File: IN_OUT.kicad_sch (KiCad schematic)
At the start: 37 parts, among them J3 Conn_DEGSON_01x02_Pin, J4 Conn_DEGSON_01x02_Pin, J5 Conn_DEGSON_01x02_Pin, J6 Conn_DEGSON_01x02_Pin, J7 Conn_DEGSON_01x02_Pin, U2 PRAG71S, U3 PRAG71S, U4 PRAG71S, U5 PRAG71S

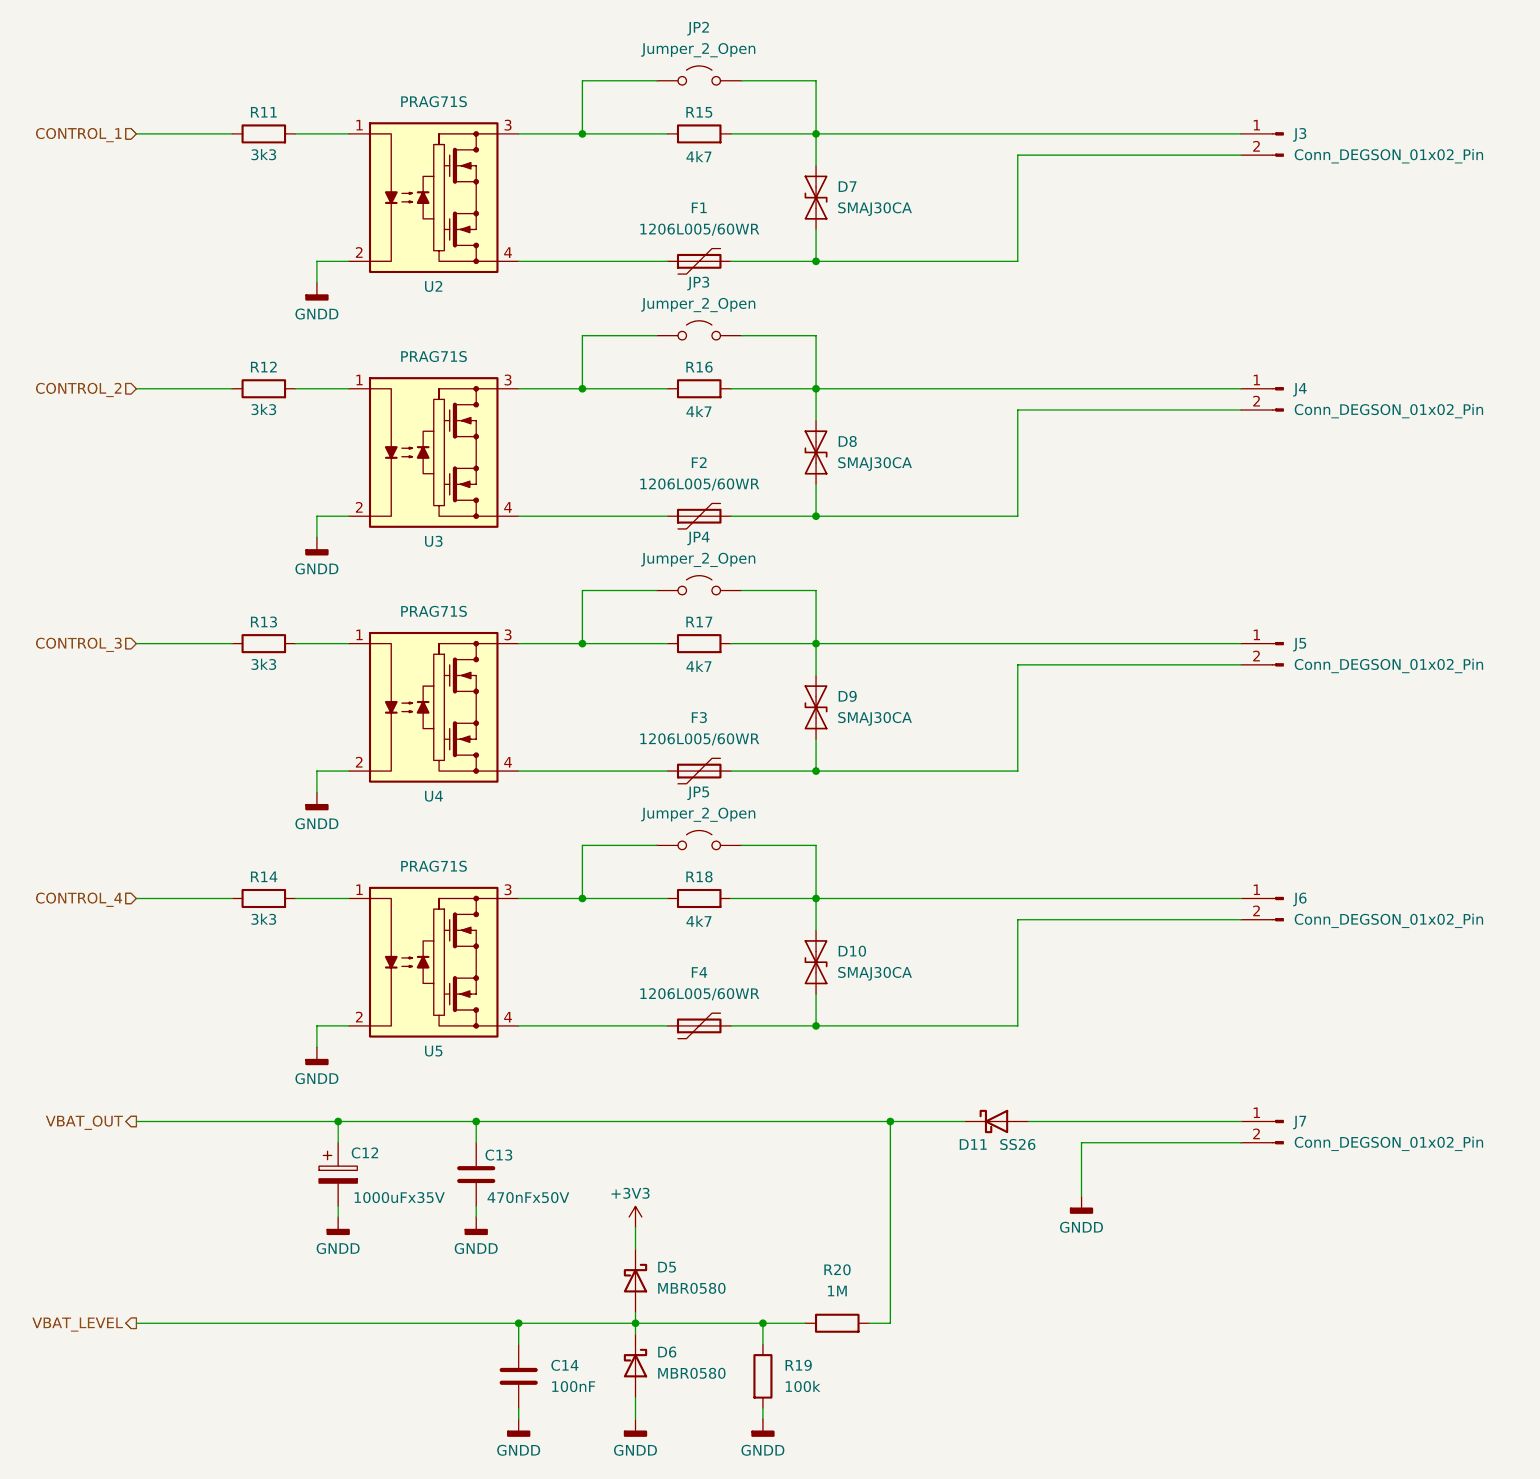
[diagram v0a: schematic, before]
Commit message: Move to SIM800C-DS and two SIM
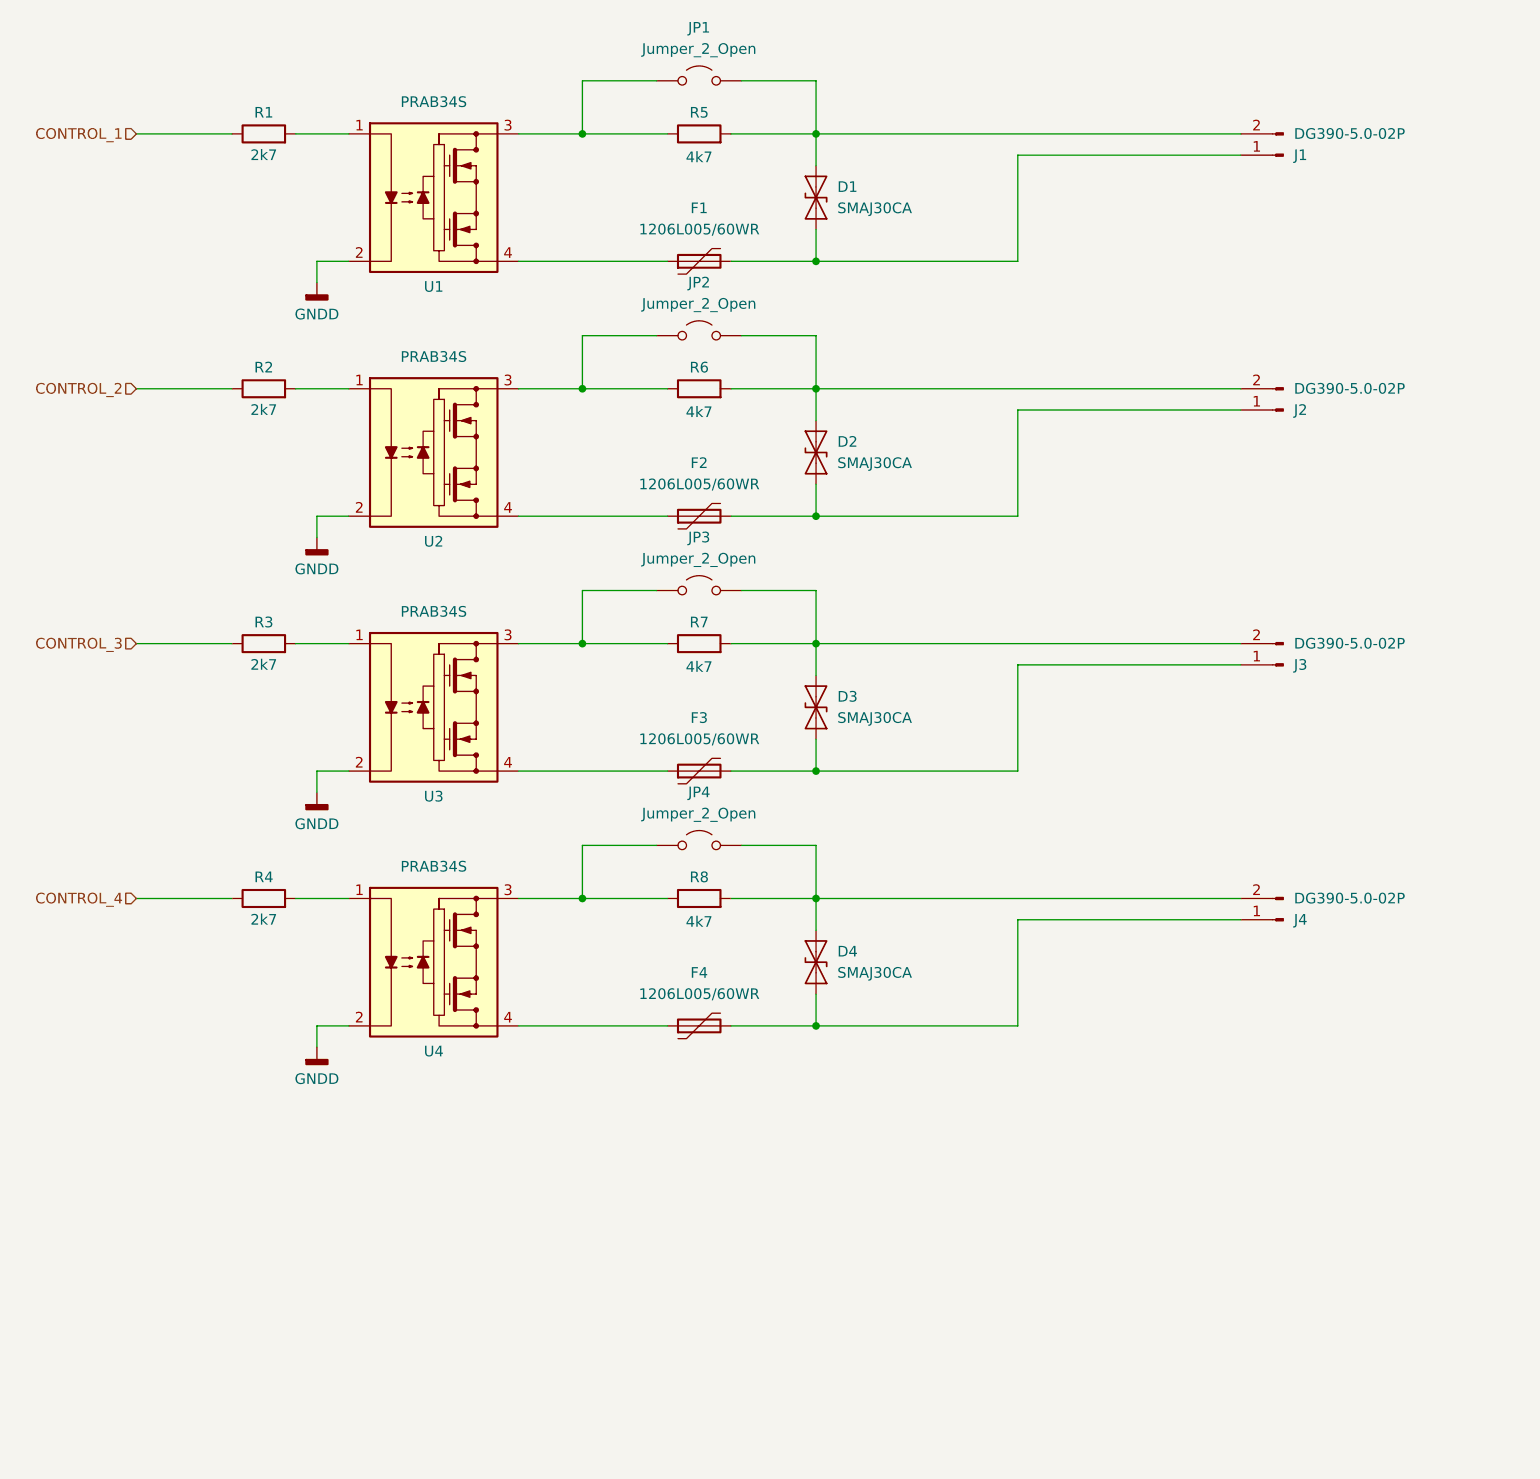
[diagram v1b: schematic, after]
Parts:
- removed C12: 1000uFx35V, Capacitor_THT:CP_Radial_D12.5mm_P5.00mm, symbol Device:C_Polarized
- removed C13: 470nFx50V, Capacitor_SMD:C_0805_2012Metric_Pad1.18x1.45mm_HandSolder, symbol Device:C
- removed C14: 100nF, Capacitor_SMD:C_0805_2012Metric_Pad1.18x1.45mm_HandSolder, symbol Device:C
- removed D11: SS26, Diode_SMD:D_SMA, symbol Diode:SS26
- removed D5, D6: MBR0580, Diode_SMD:D_SOD-123, symbol Diode:MBR0580
- removed J7: Conn_DEGSON_01x02_Pin, footprints:DEGSON_DG390-5.0-02P_1x02_P5.0mm_Vertical, symbol symbols:Conn_DEGSON_01x02_Pin
- removed R19: 100k, Resistor_SMD:R_0805_2012Metric_Pad1.20x1.40mm_HandSolder, symbol Device:R
- removed R20: 1M, Resistor_SMD:R_0805_2012Metric_Pad1.20x1.40mm_HandSolder, symbol Device:R
- D1: renamed from D7; MPN (none) -> SMAJ30CA; Manufacturer (none) -> Littelfuse
- D2: renamed from D8; MPN (none) -> SMAJ30CA; Manufacturer (none) -> Littelfuse
- D3: renamed from D9; MPN (none) -> SMAJ30CA; Manufacturer (none) -> Littelfuse
- D4: renamed from D10; MPN (none) -> SMAJ30CA; Manufacturer (none) -> Littelfuse
- F1, F2, F3, F4: MPN (none) -> 1206L005/60WR; Manufacturer (none) -> Littelfuse
- J1: renamed from J3; value Conn_DEGSON_01x02_Pin -> DG390-5.0-02P; MPN (none) -> DG390-5.0-02P; Manufacturer (none) -> NINGBO DEGSON ELECTRICAL CO.,LTD.
- J2: renamed from J4; value Conn_DEGSON_01x02_Pin -> DG390-5.0-02P; MPN (none) -> DG390-5.0-02P; Manufacturer (none) -> NINGBO DEGSON ELECTRICAL CO.,LTD.
- J3: renamed from J5; value Conn_DEGSON_01x02_Pin -> DG390-5.0-02P; MPN (none) -> DG390-5.0-02P; Manufacturer (none) -> NINGBO DEGSON ELECTRICAL CO.,LTD.
- J4: renamed from J6; value Conn_DEGSON_01x02_Pin -> DG390-5.0-02P; MPN (none) -> DG390-5.0-02P; Manufacturer (none) -> NINGBO DEGSON ELECTRICAL CO.,LTD.
- JP1: renamed from JP2; MPN (none) -> DS1021-1x2SF11-B; Manufacturer (none) -> CONNFLY ELECTRONIC CO. LTD
- JP2: renamed from JP3; MPN (none) -> DS1021-1x2SF11-B; Manufacturer (none) -> CONNFLY ELECTRONIC CO. LTD
- JP3: renamed from JP4; MPN (none) -> DS1021-1x2SF11-B; Manufacturer (none) -> CONNFLY ELECTRONIC CO. LTD
- JP4: renamed from JP5; MPN (none) -> DS1021-1x2SF11-B; Manufacturer (none) -> CONNFLY ELECTRONIC CO. LTD
- R1: renamed from R11; value 3k3 -> 2k7; MPN (none) -> RC0805JR-072K7L; Manufacturer (none) -> YAGEO
- R2: renamed from R12; value 3k3 -> 2k7; MPN (none) -> RC0805JR-072K7L; Manufacturer (none) -> YAGEO
- R3: renamed from R13; value 3k3 -> 2k7; MPN (none) -> RC0805JR-072K7L; Manufacturer (none) -> YAGEO
- R4: renamed from R14; value 3k3 -> 2k7; MPN (none) -> RC0805JR-072K7L; Manufacturer (none) -> YAGEO
- R5: renamed from R15; MPN (none) -> RC0805JR-134K7L; Manufacturer (none) -> YAGEO
- R6: renamed from R16; MPN (none) -> RC0805JR-134K7L; Manufacturer (none) -> YAGEO
- R7: renamed from R17; MPN (none) -> RC0805JR-134K7L; Manufacturer (none) -> YAGEO
- R8: renamed from R18; MPN (none) -> RC0805JR-134K7L; Manufacturer (none) -> YAGEO
- U1: renamed from U2; value PRAG71S -> PRAB34S; MPN (none) -> PRAB34S; Manufacturer (none) -> АО "Протон"
- U2: renamed from U3; value PRAG71S -> PRAB34S; MPN (none) -> PRAB34S; Manufacturer (none) -> АО "Протон"
- U3: renamed from U4; value PRAG71S -> PRAB34S; MPN (none) -> PRAB34S; Manufacturer (none) -> АО "Протон"
- U4: renamed from U5; value PRAG71S -> PRAB34S; MPN (none) -> PRAB34S; Manufacturer (none) -> АО "Протон"
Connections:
- net at D3.1 (A1), F3.2: now also J3.1 (Pin_1); no longer J3.2 (Pin_2)
- net at D4.1 (A1), F4.2: now also J4.1 (Pin_1); no longer J4.2 (Pin_2)
- net at D4.2 (A2), JP4.2 (B), R8.2: now also J4.2 (Pin_2); no longer J4.1 (Pin_1)
- net at D3.2 (A2), JP3.2 (B), R7.2: now also J3.2 (Pin_2); no longer J3.1 (Pin_1)
- net at D2.2 (A2), JP2.2 (B), R6.2: now also J2.2 (Pin_2); no longer J2.1 (Pin_1)
- net at D1.1 (A1), F1.2: now also J1.1 (Pin_1); no longer J1.2 (Pin_2)
- net at D1.2 (A2), JP1.2 (B), R5.2: now also J1.2 (Pin_2); no longer J1.1 (Pin_1)
- net at D2.1 (A1), F2.2: now also J2.1 (Pin_1); no longer J2.2 (Pin_2)
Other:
- moved on the sheet: J1, J2, J3, J4

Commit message: Release candidate
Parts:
- JP1, JP2, JP3, JP4: footprint TestPoint:TestPoint_2Pads_Pitch2.54mm_Drill0.8mm -> Connector_PinHeader_2.54mm:PinHeader_1x02_P2.54mm_Vertical
- R5, R6, R7, R8: footprint Resistor_SMD:R_0805_2012Metric_Pad1.20x1.40mm_HandSolder -> Resistor_SMD:R_1206_3216Metric_Pad1.30x1.75mm_HandSolder; MPN RC0805JR-134K7L -> RC1206JR-074K7L
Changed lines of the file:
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@@
 (kicad_sch
-	(version 20260101)
+	(version 20260306)
 	(generator "eeschema")
 	(generator_version "10.0")
@@
 			)
 		)
-		(property "Footprint" "TestPoint:TestPoint_2Pads_Pitch2.54mm_Drill0.8mm"
+		(property "Footprint" "Connector_PinHeader_2.54mm:PinHeader_1x02_P2.54mm_Vertical"
 			(at 125.73 91.44 0)
 			(hide yes)
@@
 			)
 		)
-		(property "Footprint" "Resistor_SMD:R_0805_2012Metric_Pad1.20x1.40mm_HandSolder"
+		(property "Footprint" "Resistor_SMD:R_1206_3216Metric_Pad1.30x1.75mm_HandSolder"
 			(at 125.73 69.088 90)
 			(hide yes)
@@
 			)
 		)
-		(property "MPN" "RC0805JR-134K7L"
+		(property "MPN" "RC1206JR-074K7L"
 			(at 125.73 67.31 90)
 			(hide yes)
@@
 			)
 		)
-		(property "Footprint" "TestPoint:TestPoint_2Pads_Pitch2.54mm_Drill0.8mm"
+		(property "Footprint" "Connector_PinHeader_2.54mm:PinHeader_1x02_P2.54mm_Vertical"
 			(at 125.73 60.96 0)
 			(hide yes)
@@
 			)
 		)
-		(property "Footprint" "Resistor_SMD:R_0805_2012Metric_Pad1.20x1.40mm_HandSolder"
+		(property "Footprint" "Resistor_SMD:R_1206_3216Metric_Pad1.30x1.75mm_HandSolder"
 			(at 125.73 38.608 90)
 			(hide yes)
@@
 			)
 		)
-		(property "MPN" "RC0805JR-134K7L"
+		(property "MPN" "RC1206JR-074K7L"
 			(at 125.73 36.83 90)
 			(hide yes)
@@
 			)
 		)
-		(property "Footprint" "Resistor_SMD:R_0805_2012Metric_Pad1.20x1.40mm_HandSolder"
+		(property "Footprint" "Resistor_SMD:R_1206_3216Metric_Pad1.30x1.75mm_HandSolder"
 			(at 125.73 130.048 90)
 			(hide yes)
@@
 			)
 		)
-		(property "MPN" "RC0805JR-134K7L"
+		(property "MPN" "RC1206JR-074K7L"
 			(at 125.73 128.27 90)
 			(hide yes)
@@
 			)
 		)
-		(property "Footprint" "TestPoint:TestPoint_2Pads_Pitch2.54mm_Drill0.8mm"
+		(property "Footprint" "Connector_PinHeader_2.54mm:PinHeader_1x02_P2.54mm_Vertical"
 			(at 125.73 121.92 0)
 			(hide yes)
@@
 			)
 		)
-		(property "Footprint" "TestPoint:TestPoint_2Pads_Pitch2.54mm_Drill0.8mm"
+		(property "Footprint" "Connector_PinHeader_2.54mm:PinHeader_1x02_P2.54mm_Vertical"
 			(at 125.73 30.48 0)
 			(hide yes)
@@
 			)
 		)
-		(property "Footprint" "Resistor_SMD:R_0805_2012Metric_Pad1.20x1.40mm_HandSolder"
+		(property "Footprint" "Resistor_SMD:R_1206_3216Metric_Pad1.30x1.75mm_HandSolder"
 			(at 125.73 99.568 90)
 			(hide yes)
@@
 			)
 		)
-		(property "MPN" "RC0805JR-134K7L"
+		(property "MPN" "RC1206JR-074K7L"
 			(at 125.73 97.79 90)
 			(hide yes)

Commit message: Proproduction version
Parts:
- J1: value DG390-5.0-02P -> Relay_1
- J2: value DG390-5.0-02P -> Relay_2
- J3: value DG390-5.0-02P -> Relay_3
- J4: value DG390-5.0-02P -> Relay_4
- R1, R2, R3, R4: value 2k7 -> 2.7k
- R5, R6, R7, R8: value 4k7 -> 4.7k
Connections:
- net RELAY3B: now reaches D3.1 (A1), F3.2, J3.1 (Pin_1)
- net RELAY4B: now reaches D4.1 (A1), F4.2, J4.1 (Pin_1)
- net RELAY4A: now reaches D4.2 (A2), J4.2 (Pin_2), JP4.2 (B), R8.2
- net RELAY3A: now reaches D3.2 (A2), J3.2 (Pin_2), JP3.2 (B), R7.2
- net RELAY2A: now reaches D2.2 (A2), J2.2 (Pin_2), JP2.2 (B), R6.2
- net RELAY1B: now reaches D1.1 (A1), F1.2, J1.1 (Pin_1)
- net RELAY1A: now reaches D1.2 (A2), J1.2 (Pin_2), JP1.2 (B), R5.2
- net RELAY2B: now reaches D2.1 (A1), F2.2, J2.1 (Pin_1)
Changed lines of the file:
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@@
 		)
 	)
+	(label "RELAY1A"
+		(at 153.67 36.83 0)
+		(effects
+			(font
+				(size 1.27 1.27)
+			)
+			(justify left bottom)
+		)
+	)
+	(label "RELAY4A"
+		(at 153.67 128.27 0)
+		(effects
+			(font
+				(size 1.27 1.27)
+			)
+			(justify left bottom)
+		)
+	)
+	(label "RELAY2A"
+		(at 153.67 67.31 0)
+		(effects
+			(font
+				(size 1.27 1.27)
+			)
+			(justify left bottom)
+		)
+	)
+	(label "RELAY4B"
+		(at 153.67 143.51 0)
+		(effects
+			(font
+				(size 1.27 1.27)
+			)
+			(justify left bottom)
+		)
+	)
+	(label "RELAY3B"
+		(at 153.67 113.03 0)
+		(effects
+			(font
+				(size 1.27 1.27)
+			)
+			(justify left bottom)
+		)
+	)
+	(label "RELAY3A"
+		(at 153.67 97.79 0)
+		(effects
+			(font
+				(size 1.27 1.27)
+			)
+			(justify left bottom)
+		)
+	)
+	(label "RELAY2B"
+		(at 153.67 82.55 0)
+		(effects
+			(font
+				(size 1.27 1.27)
+			)
+			(justify left bottom)
+		)
+	)
+	(label "RELAY1B"
+		(at 153.67 52.07 0)
+		(effects
+			(font
+				(size 1.27 1.27)
+			)
+			(justify left bottom)
+		)
+	)
 	(hierarchical_label "CONTROL_1"
 		(shape input)
@@
 			)
 		)
-		(property "Value" "DG390-5.0-02P"
+		(property "Value" "Relay_3"
 			(at 196.85 97.7901 0)
 			(show_name no)
@@
 			)
 		)
-		(property "Value" "4k7"
+		(property "Value" "4.7k"
 			(at 125.73 70.104 90)
 			(show_name no)
@@
 			)
 		)
-		(property "Value" "DG390-5.0-02P"
+		(property "Value" "Relay_2"
 			(at 196.85 67.3101 0)
 			(show_name no)
@@
 			)
 		)
-		(property "Value" "DG390-5.0-02P"
+		(property "Value" "Relay_1"
 			(at 196.85 36.8301 0)
 			(show_name no)
@@
 			)
 		)
-		(property "Value" "2k7"
+		(property "Value" "2.7k"
 			(at 73.66 100.33 90)
 			(show_name no)
@@
 			)
 		)
-		(property "Value" "4k7"
+		(property "Value" "4.7k"
 			(at 125.73 39.624 90)
 			(show_name no)
@@
 			)
 		)
-		(property "Value" "4k7"
+		(property "Value" "4.7k"
 			(at 125.73 131.064 90)
 			(show_name no)
@@
 			)
 		)
-		(property "Value" "2k7"
+		(property "Value" "2.7k"
 			(at 73.66 39.37 90)
 			(show_name no)
@@
 			)
 		)
-		(property "Value" "2k7"
+		(property "Value" "2.7k"
 			(at 73.66 130.81 90)
 			(show_name no)
@@
 			)
 		)
-		(property "Value" "2k7"
+		(property "Value" "2.7k"
 			(at 73.66 69.85 90)
 			(show_name no)
@@
 			)
 		)
-		(property "Value" "4k7"
+		(property "Value" "4.7k"
 			(at 125.73 100.584 90)
 			(show_name no)
@@
 			)
 		)
-		(property "Value" "DG390-5.0-02P"
+		(property "Value" "Relay_4"
 			(at 196.85 128.2701 0)
 			(show_name no)
